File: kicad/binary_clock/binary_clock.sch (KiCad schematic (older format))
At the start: 39 parts, among them J1 USB_B_Micro, J2 ISP, J3 DCF-77 Receiver, SW1 SLEEP, U3 ATmega328P-PU

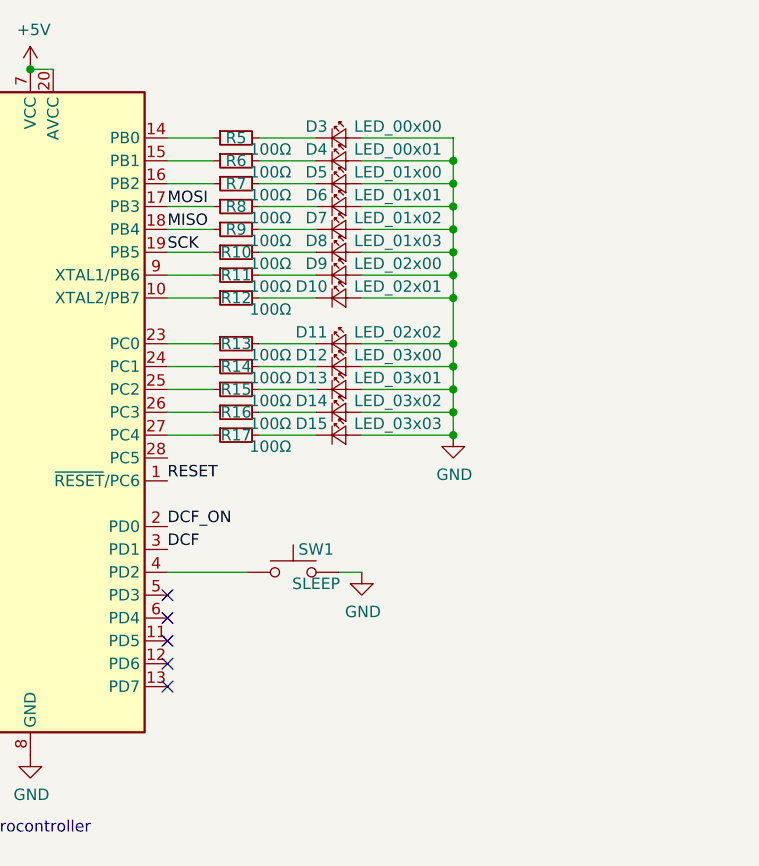
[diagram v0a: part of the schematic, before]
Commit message: Added Quarz Oscillator.
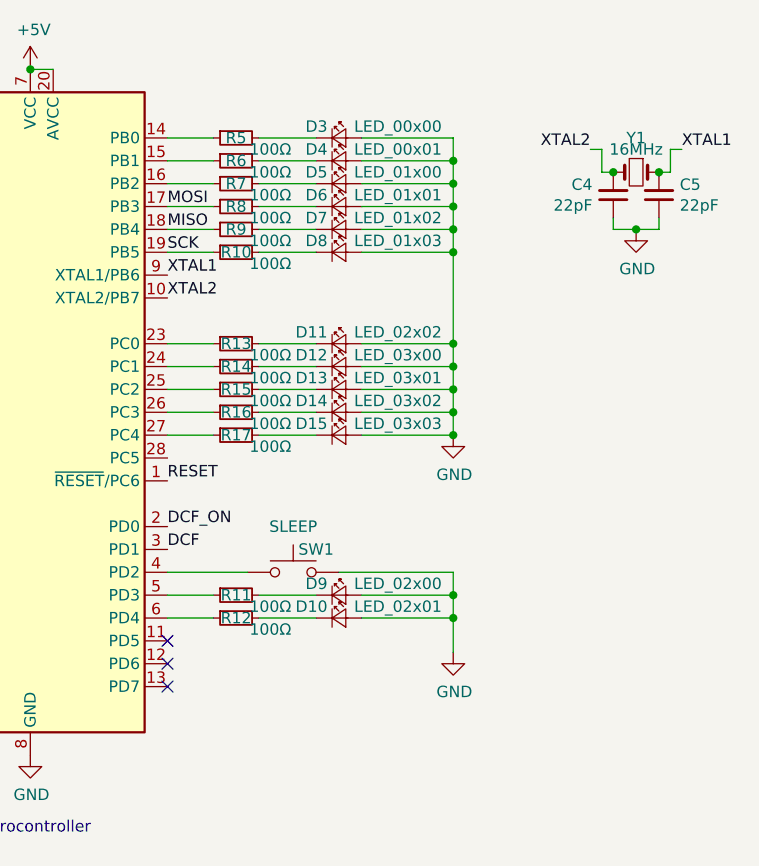
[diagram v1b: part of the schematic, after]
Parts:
- added C4, C5: 22pF, Capacitor_SMD:C_0805_2012Metric_Pad1.15x1.40mm_HandSolder, symbol Device:C_Small
- added Y1: 16MHz, Crystal:Crystal_HC49-U_Vertical, symbol Device:Crystal_Small
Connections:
- net GND: now also C4.1, C5.1
- net at R11.1: now also U3.5 (PD3); no longer U3.9 (XTAL1/PB6)
- net at R12.1: now also U3.6 (PD4); no longer U3.10 (XTAL2/PB7)
- new net XTAL1: C5.2, U3.9 (XTAL1/PB6), Y1.1
- new net XTAL2: C4.2, U3.10 (XTAL2/PB7), Y1.2
- no-connect marks 8 -> 6
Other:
- moved on the sheet: D10, D9, R11, R12
